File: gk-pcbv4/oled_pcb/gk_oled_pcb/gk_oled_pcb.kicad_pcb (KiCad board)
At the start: 4 copper layers, 50.7 x 52 mm, 48 parts, among them J2 Conn_01x01, J3 Conn_01x01, J4 Conn_01x06, J5 Conn_01x01, U1 TCA9546APW

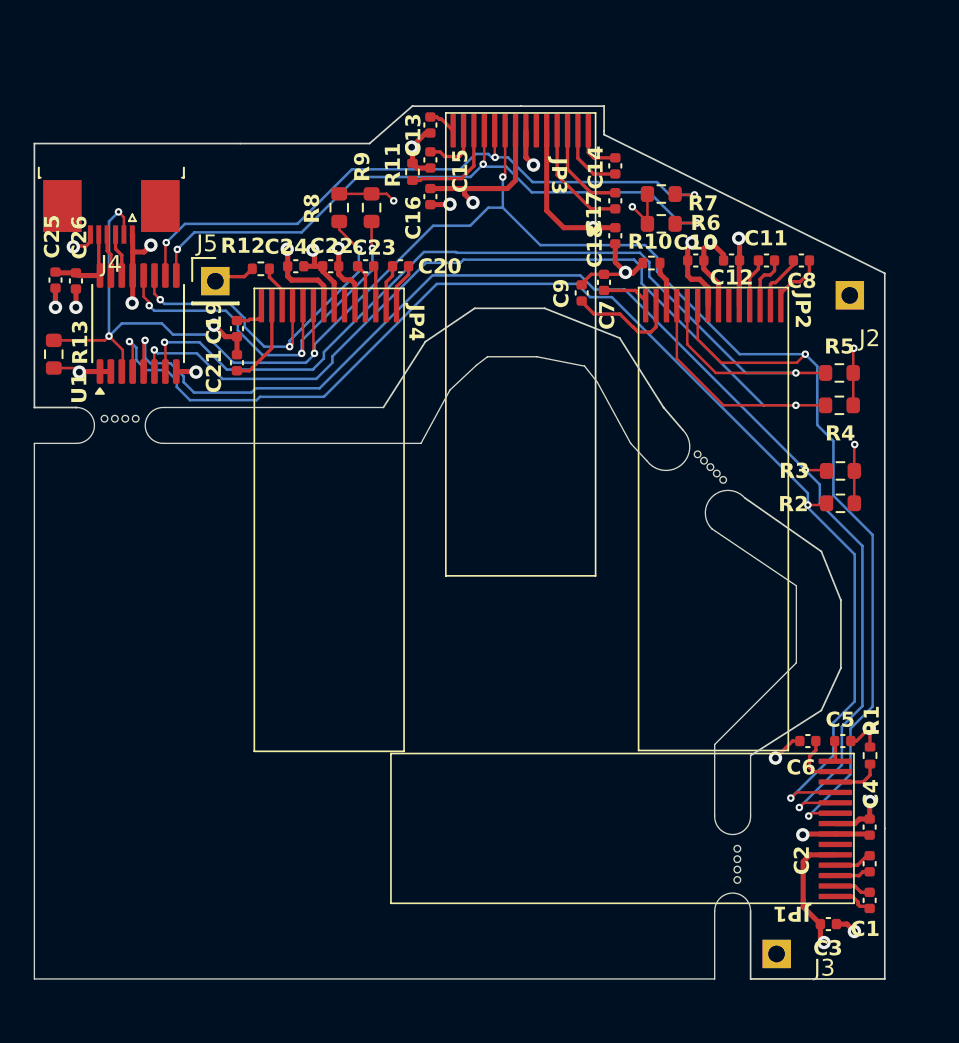
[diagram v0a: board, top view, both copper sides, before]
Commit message: begin work on adding oled board to gk
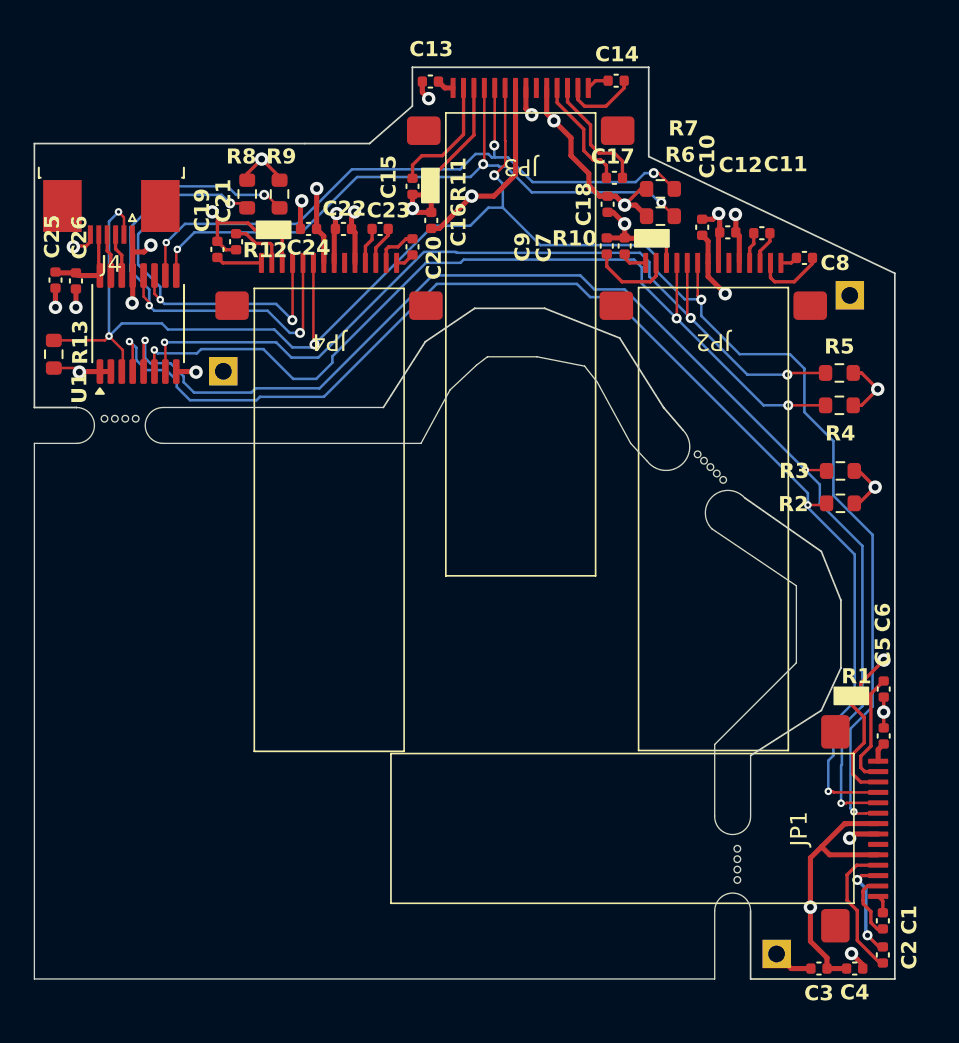
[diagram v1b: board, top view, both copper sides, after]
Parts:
- J5: moved to B.Cu
- JP1, JP2, JP3, JP4: footprint oled_lib:OLED_0_5inch_14pin -> oled_lib:FPC_0.62mm_14pin
- moved C4 8.48 mm to (143.4, 114.4), turned to 0 degrees
- moved C21 7.21 mm to (106.5, 71.0), turned to -90 degrees
- moved R8 5.55 mm to (107.2, 68.2)
- moved R9 5.55 mm to (109.1, 68.2)
- moved C2 5.49 mm to (145.1, 113.5), turned to -90 degrees
- moved C6 5.48 mm to (145.1, 97.7), turned to -90 degrees
- moved J5 5.39 mm to (105.8, 78.7), turned to 180 degrees
- moved C14 5.08 mm to (129.2, 61.4), turned to 0 degrees
- moved C19 4.87 mm to (105.4, 71.5), turned to 90 degrees
- moved R1 3.66 mm to (143.3, 98.1), turned to 0 degrees
- moved C9 3.17 mm to (128.6, 71.3)
- moved C3 2.71 mm to (141.3, 114.4), turned to 180 degrees
- moved C13 2.59 mm to (118.1, 61.5), turned to 180 degrees
- moved C7 2.49 mm to (129.7, 71.3)
- moved C5 2.46 mm to (145.1, 100.5), turned to 90 degrees
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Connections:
- J5 pad 1: GND -> (no net)
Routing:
- net SCL4: track 24.1 -> 31.4 mm
- net SDA2: track 59.8 -> 52.9 mm, vias 2 -> 3
- net SCL2: track 57.0 -> 50.8 mm, vias 2 -> 3
- net Net-(JP1-C1N): track 2.28 -> 8.34 mm
- net VCC: track 62.3 -> 67.7 mm, vias 13 -> 12
- net Net-(JP1-IREF): track 2.90 -> 7.09 mm
- net Net-(JP1-C1P): track 2.14 -> 6.11 mm, vias 0 -> 2
- net Net-(JP3-VCOMH): track 3.48 -> 7.36 mm
- net SDA4: track 21.9 -> 25.6 mm
- net Net-(JP1-VCOMH): track 3.37 -> 6.87 mm
- net Net-(JP2-C2P): track 3.67 -> 1.05 mm
- net GND: track 51.1 -> 48.8 mm, vias 17 -> 18
- net OLED_NRES: track 113.2 -> 110.9 mm
- net Net-(JP1-C2N): track 2.20 -> 3.99 mm
- net Net-(JP3-C2P): track 3.04 -> 1.36 mm
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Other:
- board size 50.7 x 52 mm -> 51.3 x 54.4 mm
